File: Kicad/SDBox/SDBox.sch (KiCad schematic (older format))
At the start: 25 parts, among them J1 Amiga Parallel port, J2 PROG, J3 SD_Card, J4 USB_B_Micro, J5 USB_B_Mini, J6 POWER, U1 ATmega328-AU, U2 SPX3819M5-L-3-3, Y1 16M

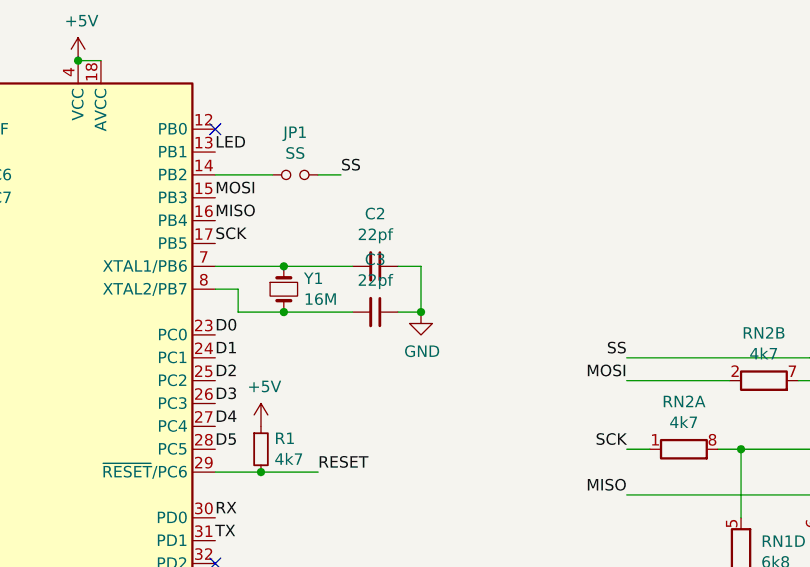
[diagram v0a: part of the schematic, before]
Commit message: Added CSTCE crystal footprint
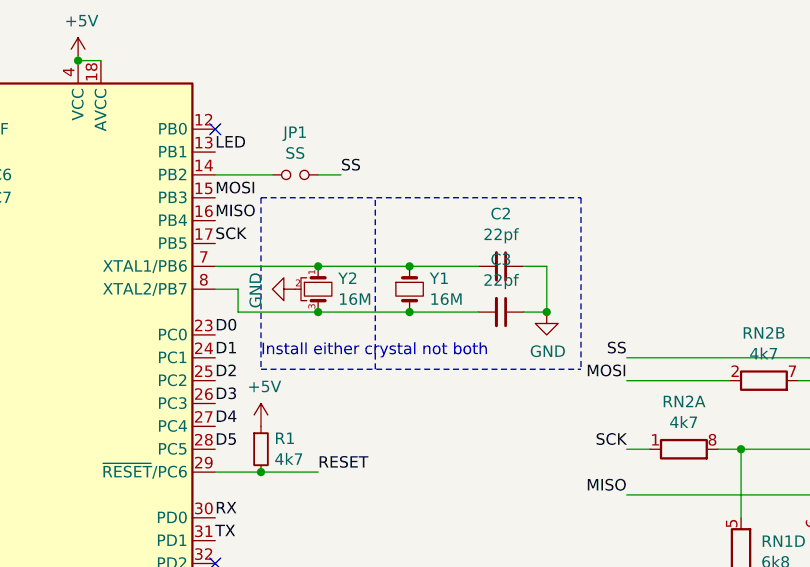
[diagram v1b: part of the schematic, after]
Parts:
- added Y2: 16M, Sassa:MURATA_CSTCE, symbol Device:Crystal_GND2_Small
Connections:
- net GND: now also Y2.2
- net at C2.2, U1.7 (XTAL1/PB6), Y1.1: now also Y2.1
- net at C3.2, U1.8 (XTAL2/PB7), Y1.2: now also Y2.3
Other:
- note added: "Install either crystal not both"
- moved on the sheet: C2, C3, Y1
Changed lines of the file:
@@
 L Device:Crystal_Small Y1
 U 1 1 5EF229CC
-P 5450 3500
-F 0 "Y1" V 5404 3588 50  0000 L CNN
-F 1 "16M" V 5495 3588 50  0000 L CNN
-F 2 "Crystal:Crystal_SMD_HC49-SD" H 5450 3500 50  0001 C CNN
-F 3 "~" H 5450 3500 50  0001 C CNN
-	1    5450 3500
+P 6000 3500
+F 0 "Y1" V 5954 3588 50  0000 L CNN
+F 1 "16M" V 6045 3588 50  0000 L CNN
+F 2 "Crystal:Crystal_SMD_HC49-SD" H 6000 3500 50  0001 C CNN
+F 3 "~" H 6000 3500 50  0001 C CNN
+	1    6000 3500
 	0    1    1    0
 $EndComp
@@
 L Device:C_Small C2
 U 1 1 5EF23676
-P 5850 3400
-F 0 "C2" V 5621 3400 50  0000 C CNN
-F 1 "22pf" V 5712 3400 50  0000 C CNN
-F 2 "Capacitor_SMD:C_0805_2012Metric" H 5850 3400 50  0001 C CNN
-F 3 "~" H 5850 3400 50  0001 C CNN
-	1    5850 3400
+P 6400 3400
+F 0 "C2" V 6171 3400 50  0000 C CNN
+F 1 "22pf" V 6262 3400 50  0000 C CNN
+F 2 "Capacitor_SMD:C_0805_2012Metric" H 6400 3400 50  0001 C CNN
+F 3 "~" H 6400 3400 50  0001 C CNN
+	1    6400 3400
 	0    1    1    0
 $EndComp
@@
 L Device:C_Small C3
 U 1 1 5EF23BA2
-P 5850 3600
-F 0 "C3" V 5621 3600 50  0000 C CNN
-F 1 "22pf" V 5712 3600 50  0000 C CNN
-F 2 "Capacitor_SMD:C_0805_2012Metric" H 5850 3600 50  0001 C CNN
-F 3 "~" H 5850 3600 50  0001 C CNN
-	1    5850 3600
+P 6400 3600
+F 0 "C3" V 6171 3600 50  0000 C CNN
+F 1 "22pf" V 6262 3600 50  0000 C CNN
+F 2 "Capacitor_SMD:C_0805_2012Metric" H 6400 3600 50  0001 C CNN
+F 3 "~" H 6400 3600 50  0001 C CNN
+	1    6400 3600
 	0    1    1    0
 $EndComp
@@
 L power:GND #PWR06
 U 1 1 5EF242F6
-P 6050 3600
-F 0 "#PWR06" H 6050 3350 50  0001 C CNN
-F 1 "GND" H 6055 3427 50  0000 C CNN
-F 2 "" H 6050 3600 50  0001 C CNN
-F 3 "" H 6050 3600 50  0001 C CNN
-	1    6050 3600
-	1    0    0    -1
-$EndComp
-Wire Wire Line
-	5150 3400 5450 3400
-Connection ~ 5450 3400
-Wire Wire Line
-	5450 3400 5750 3400
-Wire Wire Line
-	5950 3400 6050 3400
-Wire Wire Line
-	6050 3400 6050 3600
-Wire Wire Line
-	6050 3600 5950 3600
-Connection ~ 6050 3600
-Wire Wire Line
-	5750 3600 5450 3600
+P 6600 3600
+F 0 "#PWR06" H 6600 3350 50  0001 C CNN
+F 1 "GND" H 6605 3427 50  0000 C CNN
+F 2 "" H 6600 3600 50  0001 C CNN
+F 3 "" H 6600 3600 50  0001 C CNN
+	1    6600 3600
+	1    0    0    -1
+$EndComp
+Wire Wire Line
+	5150 3400 5600 3400
+Connection ~ 6000 3400
+Wire Wire Line
+	6000 3400 6300 3400
+Wire Wire Line
+	6500 3400 6600 3400
+Wire Wire Line
+	6600 3600 6500 3600
+Connection ~ 6600 3600
+Wire Wire Line
+	6300 3600 6000 3600
 Wire Wire Line
 	5250 3600 5250 3500
 Wire Wire Line
 	5250 3500 5150 3500
-Connection ~ 5450 3600
-Wire Wire Line
-	5450 3600 5250 3600
+Connection ~ 6000 3600
+Wire Wire Line
+	6000 3600 5600 3600
 $Comp
 L Connector:DB25_Male J1
@@
 Text Label 5150 2900 0    50   ~ 0
 LED
+$Comp
+L Device:Crystal_GND2_Small Y2
+U 1 1 5F6BEFF7
+P 5600 3500
+F 0 "Y2" V 5554 3588 50  0000 L CNN
+F 1 "16M" V 5645 3588 50  0000 L CNN
+F 2 "Sassa:MURATA_CSTCE" H 5600 3500 50  0001 C CNN
+F 3 "~" H 5600 3500 50  0001 C CNN
+	1    5600 3500
+	0    1    1    0
+$EndComp
+Wire Wire Line
+	6600 3400 6600 3600
+Connection ~ 5600 3400
+Wire Wire Line
+	5600 3400 6000 3400
+Connection ~ 5600 3600
+Wire Wire Line
+	5600 3600 5250 3600
+$Comp
+L power:GND #PWR?
+U 1 1 5F6E0DFE
+P 5500 3500
+F 0 "#PWR?" H 5500 3250 50  0001 C CNN
+F 1 "GND" H 5505 3327 50  0000 C CNN
+F 2 "" H 5500 3500 50  0001 C CNN
+F 3 "" H 5500 3500 50  0001 C CNN
+	1    5500 3500
+	0    1    1    0
+$EndComp
+Wire Notes Line
+	5350 3100 5350 3850
+Wire Notes Line
+	5850 3850 5850 3100
+Wire Notes Line
+	6750 3100 6750 3850
+Wire Notes Line
+	5350 3850 6750 3850
+Wire Notes Line
+	5350 3100 6750 3100
+Text Notes 5350 3800 0    50   ~ 0
+Install either crystal not both
 $EndSCHEMATC

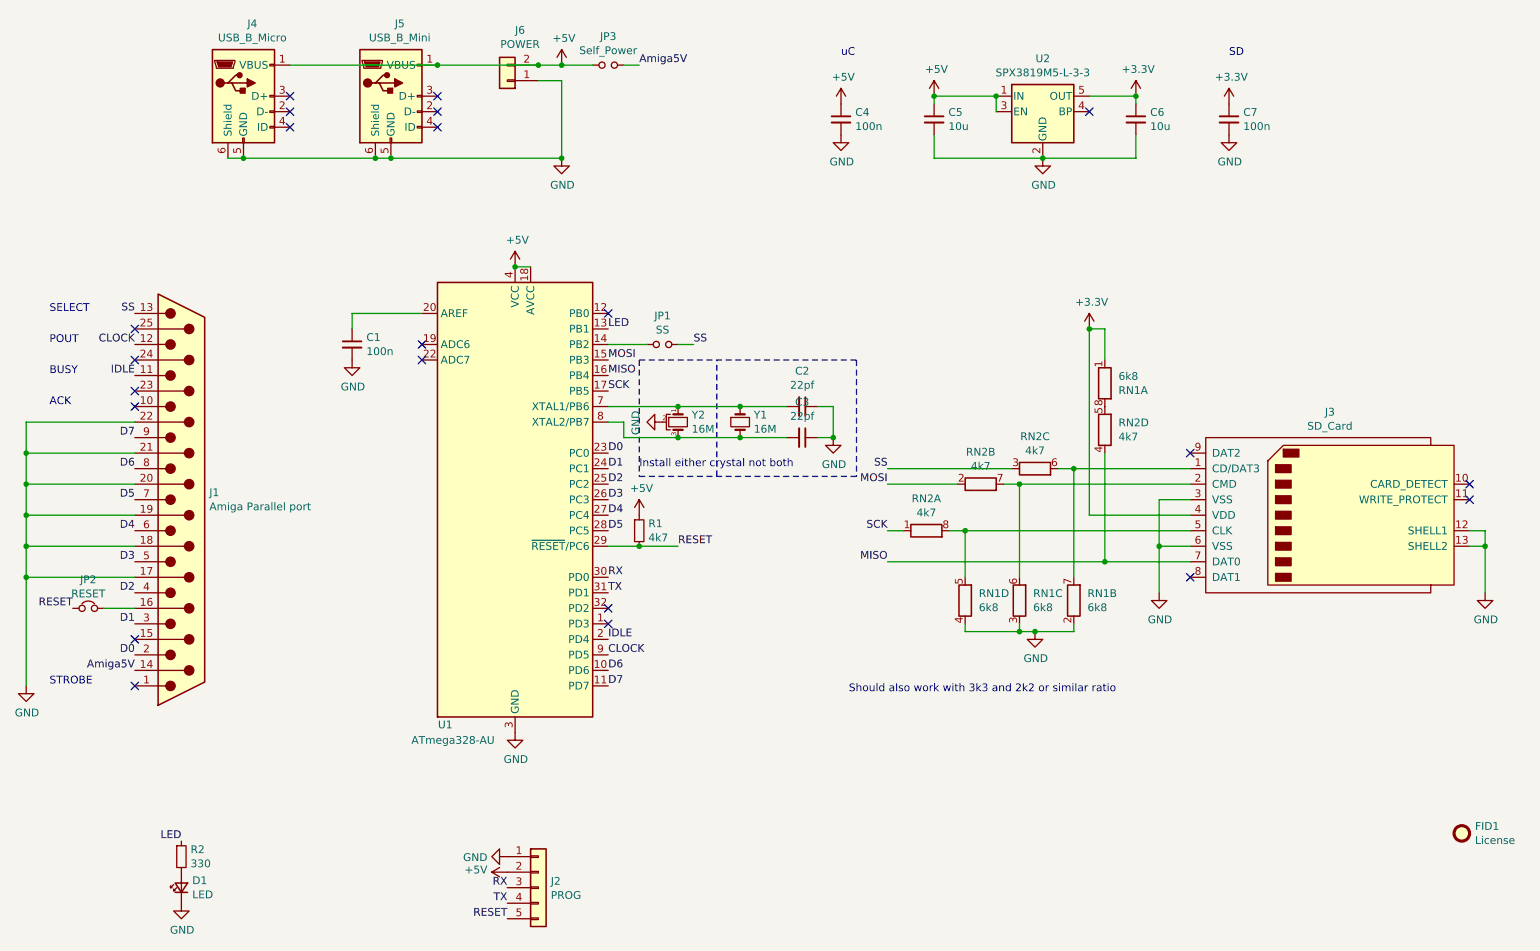
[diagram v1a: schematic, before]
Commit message: Kicad : 0.2 with broken SPI programming port
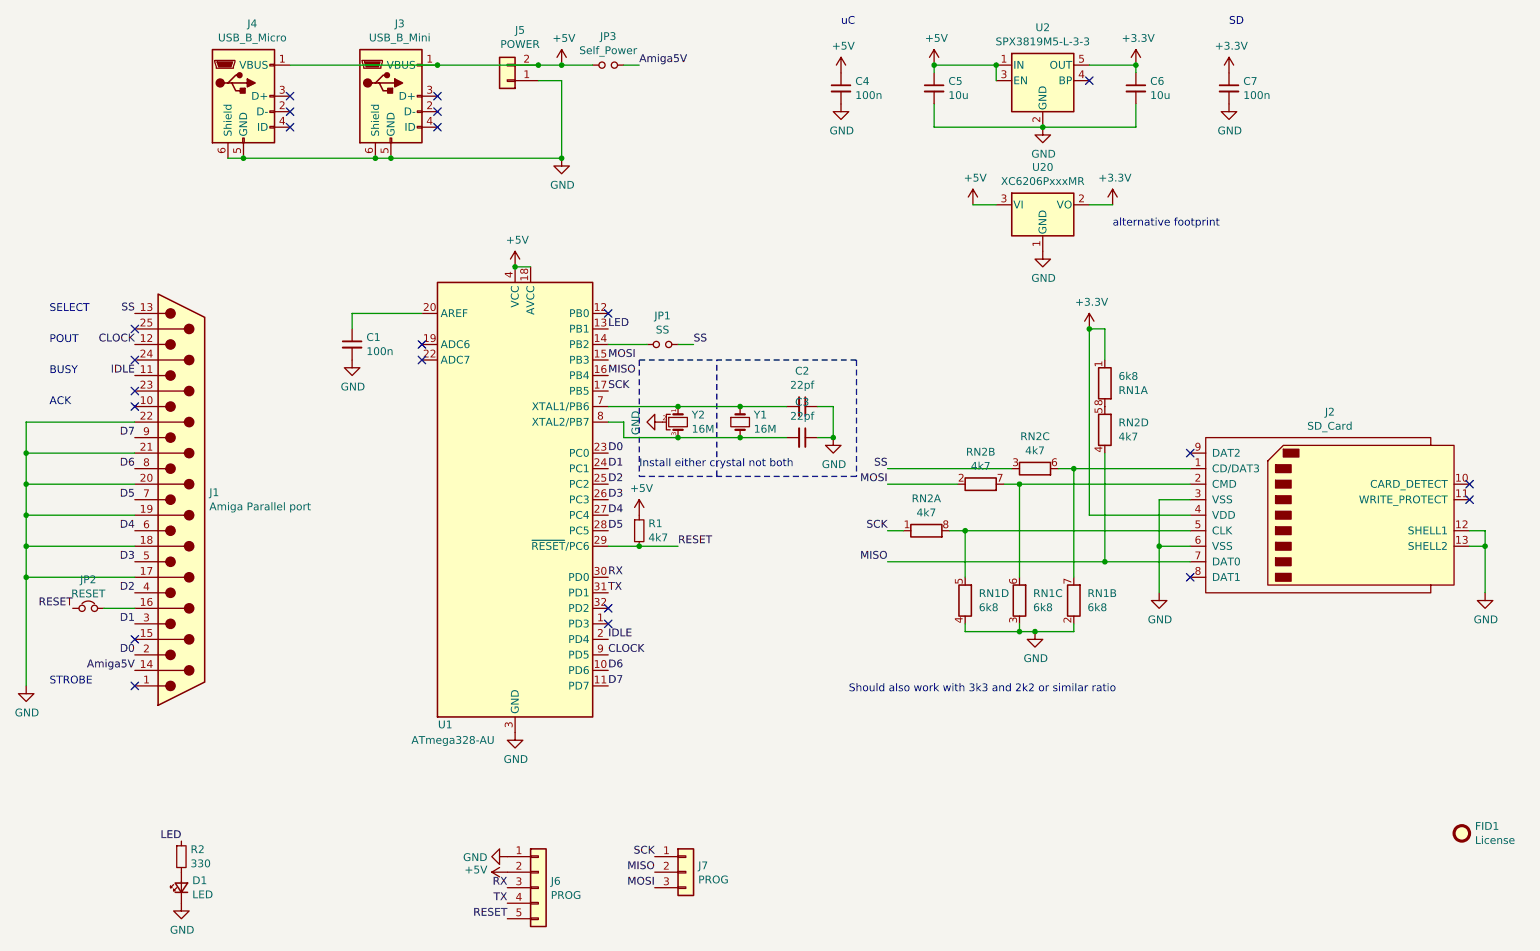
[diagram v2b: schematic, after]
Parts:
- added J7: PROG, Connector_PinHeader_2.54mm:PinHeader_1x03_P2.54mm_Vertical, symbol Connector_Generic:Conn_01x03
- added U20: XC6206PxxxMR, Package_TO_SOT_SMD:SOT-23, symbol Regulator_Linear:XC6206PxxxMR
- renumbered J3 to J2, J5 to J3, J6 to J5, J2 to J6
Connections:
- net +3V3: now also U20.2 (VO)
- net +5V: now also U20.3 (VI)
- net GND: now also U20.1 (GND)
- net MISO: now also J7.2 (Pin_2)
- net MOSI: now also J7.3 (Pin_3)
- net SCK: now also J7.1 (Pin_1)
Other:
- note added: "alternative footprint"
- moved on the sheet: C4, C5, C6, C7, U2
